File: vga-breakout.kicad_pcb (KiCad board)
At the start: 2 copper layers, 46 x 26 mm, 8 parts, among them J1 DE15_Socket_HighDensity_Mount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, J2 Conn_01x11_Pin, J3 USB_C_Receptacle_PowerOnly_6P, SW1 SW_SPDT_321

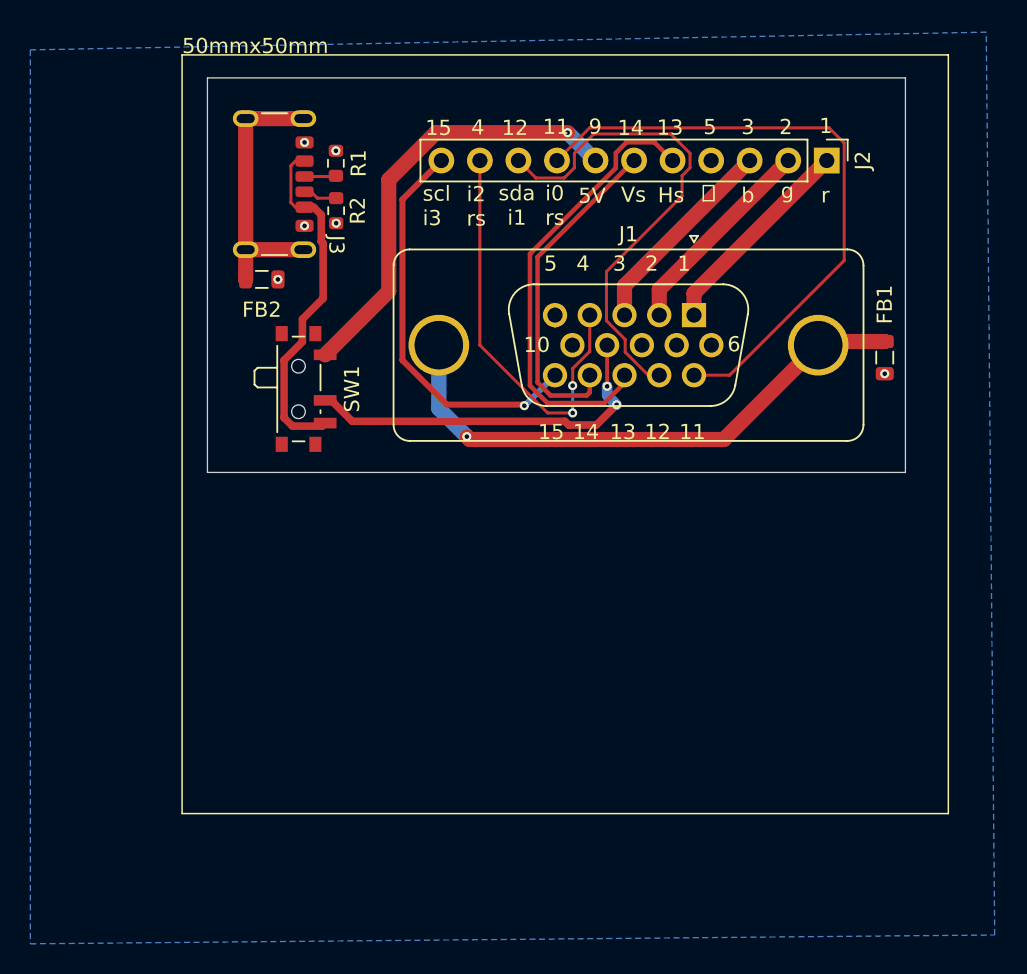
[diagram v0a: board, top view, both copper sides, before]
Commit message: remove ferrite from sheilding, rerouting
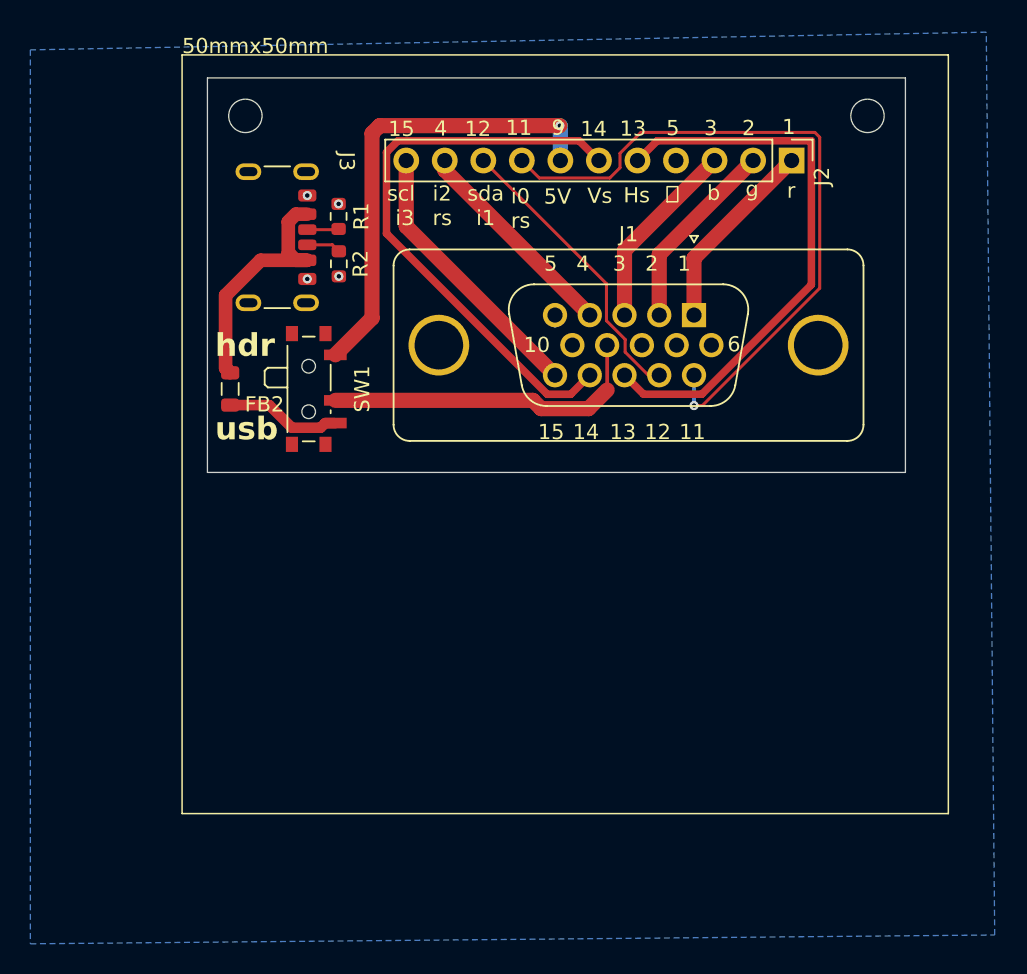
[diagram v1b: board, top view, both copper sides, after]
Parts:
- removed FB1: FerriteBead_Small, Inductor_SMD:L_0805_2012Metric
- added REF**: MountingHole_2.2mm_M2, MountingHole:MountingHole_2.2mm_M2, F.Cu at (72.5, 92.0)
- added REF**: MountingHole_2.2mm_M2, MountingHole:MountingHole_2.2mm_M2, F.Cu at (113.5, 92.0)
- moved FB2 7.51 mm to (71.5, 110.0), turned to 90 degrees
- moved J3 3.50 mm to (73.5, 100.0)
- moved R1 3.50 mm to (78.6, 98.6)
- moved R2 3.50 mm to (78.7, 101.8)
- moved J2 2.32 mm to (108.5, 94.9)
- moved SW1 0.67 mm to (77.0, 110.0)
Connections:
- FB2 pad 1: Net-(J3-SHIELD) -> Net-(SW1-A)
- FB2 pad 2: GND -> /u5v
- J1 pad 0: Net-(FB1-Pad2) -> GND
- J3 pad S1: Net-(J3-SHIELD) -> GND
- SW1 pad 3: /u5v -> Net-(SW1-A)
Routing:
- net Net-(FB1-Pad2): track 37.8 -> 0.00 mm, vias 1 -> 0
- net Net-(J3-SHIELD): track 18.2 -> 0.00 mm
- net /vs: track 22.3 -> 38.5 mm
- net /id1/sda: track 32.8 -> 19.4 mm
- net /id2/res: track 27.1 -> 14.1 mm, vias 2 -> 0
- net /id3/scl: track 26.4 -> 18.2 mm, vias 1 -> 0
- net Net-(SW1-A): track 0.00 -> 7.67 mm
- net /HS: track 30.0 -> 37.3 mm
- net /u5v: track 23.3 -> 16.5 mm
- net /id0/res: track 41.0 -> 45.5 mm, vias 0 -> 1
- net /5V: track 24.6 -> 21.6 mm, vias 2 -> 0
- net /green: track 13.7 -> 12.7 mm
- net /red: track 13.8 -> 12.9 mm
- net /blue: track 13.6 -> 12.6 mm
- net /h5v: track 29.7 -> 30.5 mm
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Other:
- board text added: "hdr"
- board text added: "usb"

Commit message: add tvs diode, reroute
reroute with vias only for 5V trace
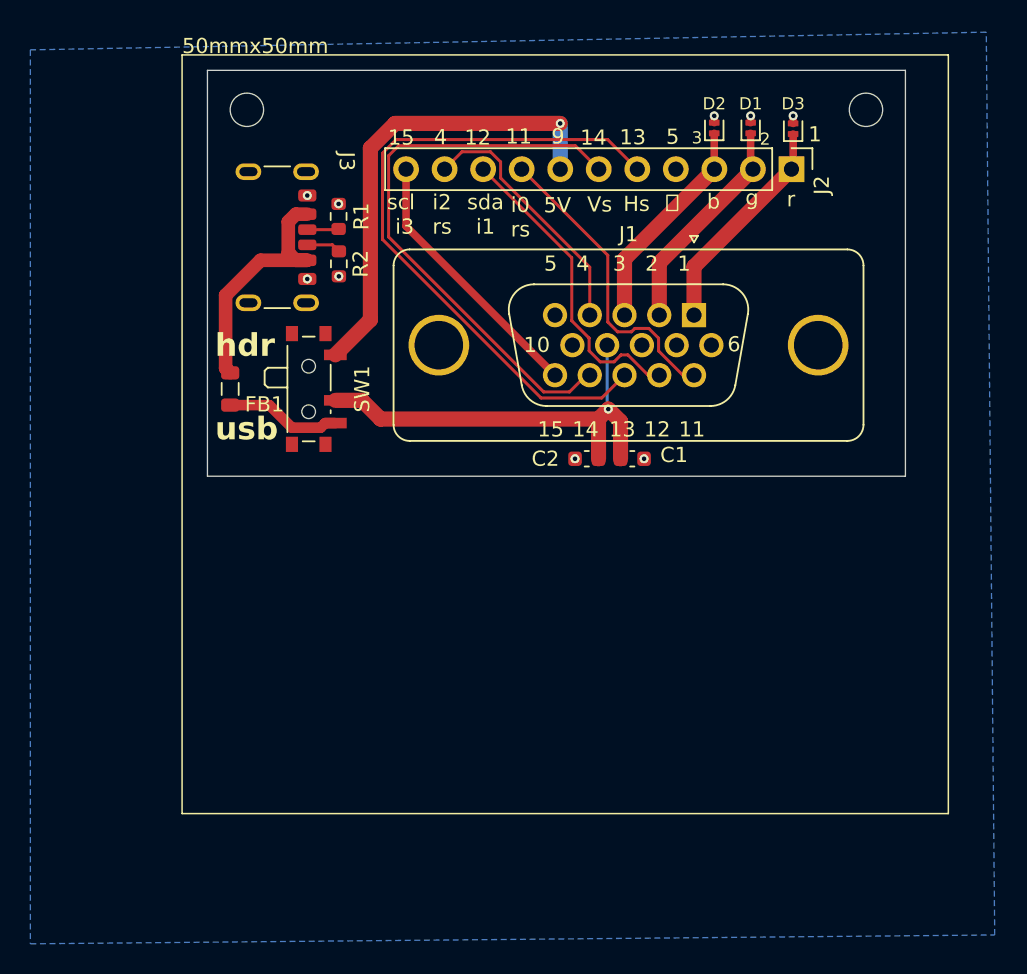
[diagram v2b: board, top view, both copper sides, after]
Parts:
- added C1: C, Capacitor_SMD:C_0603_1608Metric, F.Cu at (98.0, 114.6)
- added C2: C, Capacitor_SMD:C_0603_1608Metric, F.Cu at (95.0, 114.6)
- added D1: PESD5V0L1UL, Diode_SMD:D_SOD-882, F.Cu at (105.8, 92.8)
- added D2: PESD5V0L1UL, Diode_SMD:D_SOD-882, F.Cu at (103.4, 92.8)
- added D3: PESD5V0L1UL, Diode_SMD:D_SOD-882, F.Cu at (108.6, 92.8)
- moved J2 0.57 mm to (108.5, 95.5)
- moved REF** 0.41 mm to (72.6, 91.6)
- moved REF** 0.41 mm to (113.4, 91.6)
- renumbered FB2 to FB1
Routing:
- net /id0/res: track 45.5 -> 20.2 mm, vias 1 -> 0
- net /5V: track 21.6 -> 29.2 mm, vias 0 -> 1
- net /HS: track 37.3 -> 44.6 mm
- net /id2/res: track 14.1 -> 17.0 mm
- net /blue: track 12.6 -> 15.0 mm
- net /green: track 12.7 -> 14.6 mm
- net /red: track 12.9 -> 14.6 mm
- net /id1/sda: track 19.4 -> 20.5 mm
- net /id3/scl: track 18.2 -> 17.6 mm
- net GND: track 1.54 -> 1.40 mm, vias 4 -> 9
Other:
- board size 46 x 26 mm -> 46 x 26.8 mm
